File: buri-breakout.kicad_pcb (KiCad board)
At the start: 2 copper layers, 94 x 61 mm, 7 parts, among them P1 PWR, P2 D[0..7], P3 CTRL, P4 Buri-Bus, P5 A[0..7], P6 A[8..15], P7 A[15..23]

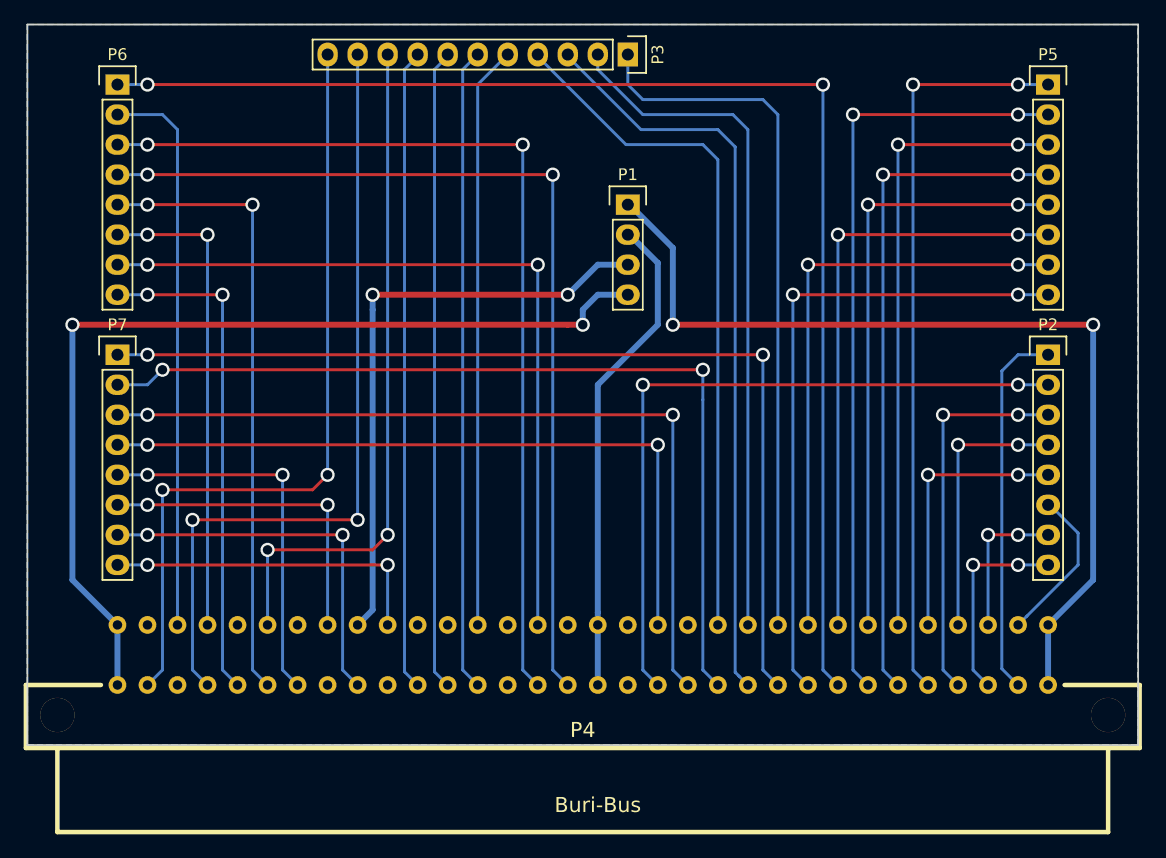
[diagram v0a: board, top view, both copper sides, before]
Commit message: Increase via size
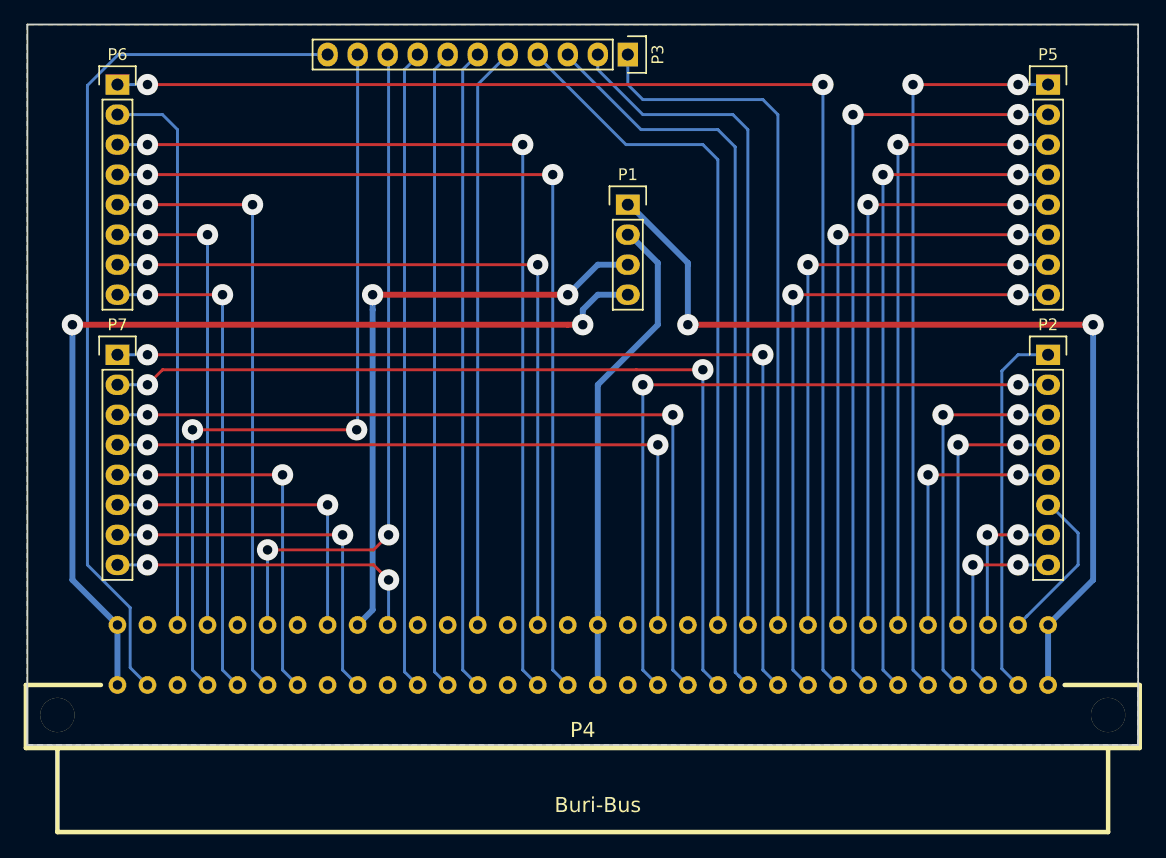
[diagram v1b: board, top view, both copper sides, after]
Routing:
- net /~RST: track 67.3 -> 74.2 mm, vias 2 -> 0
- net +5V: track 79.4 -> 78.7 mm
- net /A23: track 27.9 -> 27.3 mm
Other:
- net class Default: via_dia 1.2 -> 1.8
- net class PWR: via_dia 1.2 -> 1.8

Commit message: Re-draw PCB
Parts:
- moved P6 54.7 mm to (142.2, 76.2), turned to 180 degrees
- moved P1 30.7 mm to (106.7, 53.3), turned to 180 degrees
- moved P7 25.5 mm to (116.8, 76.2), turned to 180 degrees
- moved P2 25.5 mm to (167.6, 53.3), turned to 180 degrees
- moved P5 20.5 mm to (167.6, 76.2), turned to 180 degrees
- moved P3 7.62 mm to (142.2, 53.3)
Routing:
- net GND: track 80.8 -> 0.00 mm, vias 2 -> 0
- net /A8: track 111.0 -> 42.4 mm
- net /D7: track 17.1 -> 82.3 mm, vias 2 -> 4
- net /D6: track 12.8 -> 78.0 mm, vias 2 -> 4
- net /D4: track 22.9 -> 81.4 mm, vias 2 -> 4
- net +3V3: track 41.3 -> 97.6 mm, vias 0 -> 2
- net /D5: track 13.4 -> 67.8 mm, vias 0 -> 4
- net /A11: track 80.5 -> 34.8 mm
- net /A10: track 80.5 -> 39.9 mm
- net /A14: track 66.0 -> 25.4 mm, vias 2 -> 0
- net /~IOSEL: track 58.0 -> 96.7 mm, vias 2 -> 4
- net +5V: track 78.7 -> 116.9 mm
- net /5VBat: track 51.1 -> 83.7 mm, vias 2 -> 4
- net /D3: track 22.9 -> 49.4 mm, vias 2 -> 0
- net /A3: track 57.7 -> 31.5 mm, vias 2 -> 0
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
